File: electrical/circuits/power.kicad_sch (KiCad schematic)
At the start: 0 parts

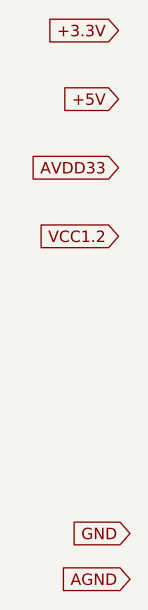
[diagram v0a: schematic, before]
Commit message: Updated circuit schematics for 10BASE-T SNI mode
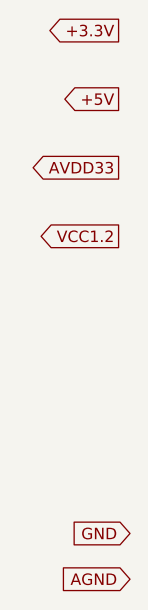
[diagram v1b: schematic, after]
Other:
- title: (none) -> Free Space Optical 10BASE-T Ethernet Transceiver Circuit
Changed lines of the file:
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@@
 	(paper "A")
 	(title_block
-		(date "2025-07-15")
+		(title "Free Space Optical 10BASE-T Ethernet Transceiver Circuit")
+		(date "2025-07-22")
 	)
 	(global_label "VCC1.2"
-		(shape input)
+		(shape output)
 		(at 83.82 90.17 180)
 		(fields_autoplaced yes)
@@
 	)
 	(global_label "+3.3V"
-		(shape input)
+		(shape output)
 		(at 83.82 67.31 180)
 		(fields_autoplaced yes)
@@
 	)
 	(global_label "+5V"
-		(shape input)
+		(shape output)
 		(at 83.82 74.93 180)
 		(fields_autoplaced yes)
@@
 	)
 	(global_label "AVDD33"
-		(shape input)
+		(shape output)
 		(at 83.82 82.55 180)
 		(fields_autoplaced yes)
